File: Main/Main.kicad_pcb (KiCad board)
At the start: 4 copper layers, 76.2 x 64.9 mm, 97 parts, among them J1 USB_B_Micro, J2 XT60, J3 Conn_01x03, J4 Conn_01x03, J5 Conn_01x03, J6 Conn_01x03, J7 MSD-4-A, J9 Conn_01x03, Q2 Si2301CDS, SW1 SW_Push, SW2 SW_Push, U1 RP2350A-QFN60, U10 LM75B, U11 MCS1802GS-50-Z, U12 MCS1802GS-50-Z, U13 MCS1802GS-50-Z, U15 AP62150WU, U2 W25Q128JVS, U3 AMS1117-3.3, U4 MMC5983MA, U5 ICM-42688-P, U6 INA226, U7 KX134-1211, U8 MS5611-01BA, U9 MCS1802GS-50-Z, Y1 ABM8-272-T3

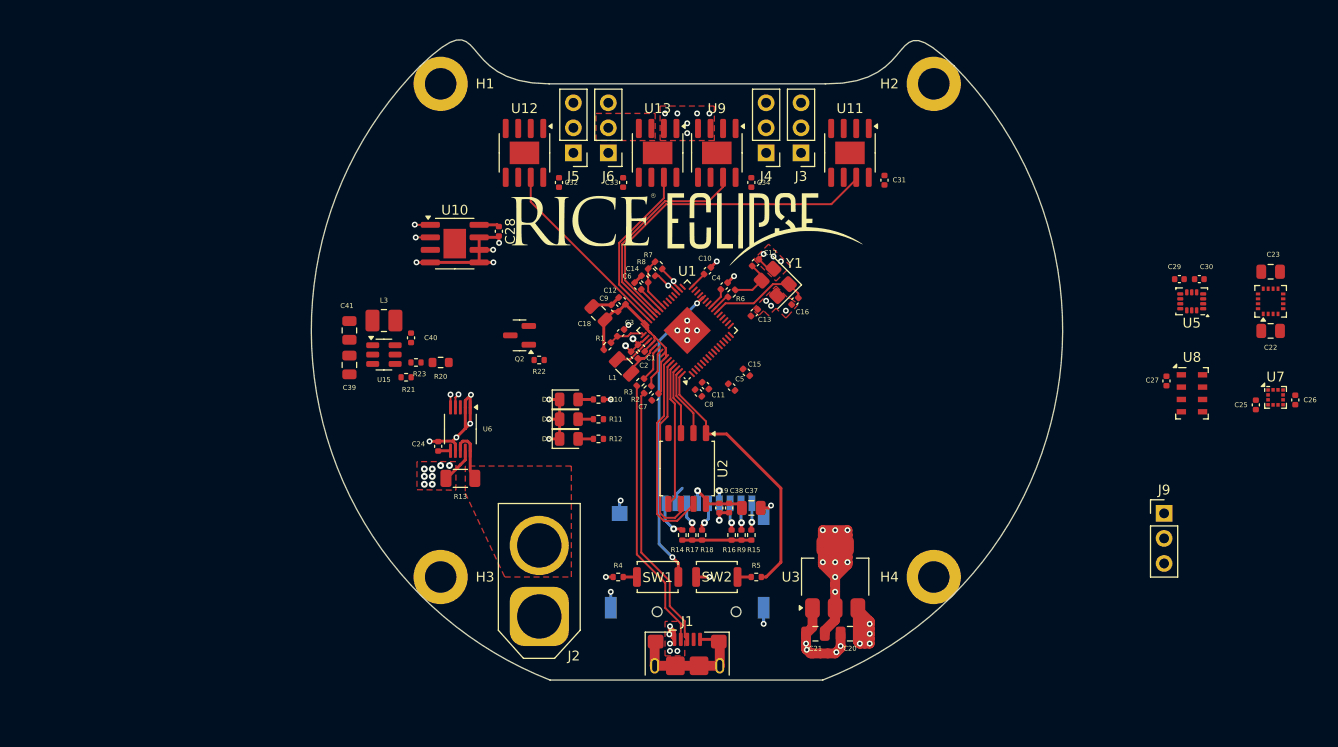
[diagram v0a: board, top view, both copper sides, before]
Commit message: Power Reg Layout Complete
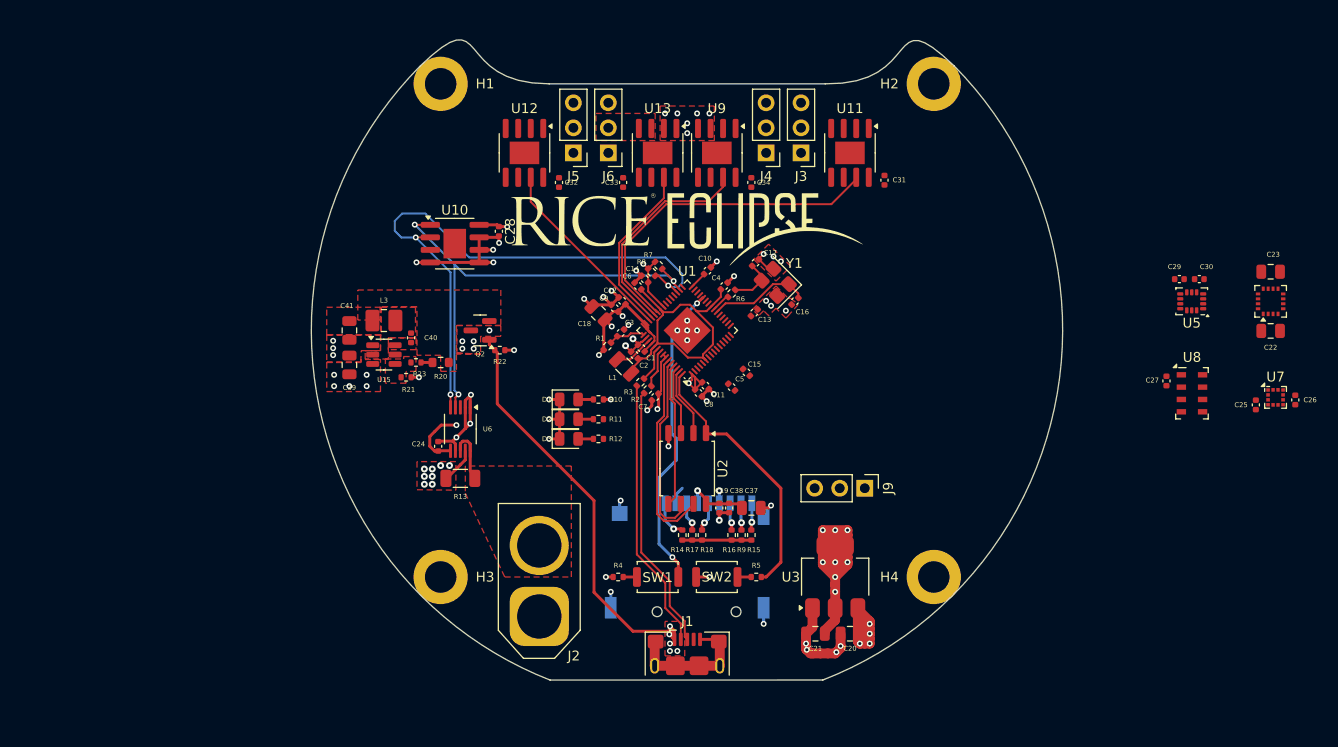
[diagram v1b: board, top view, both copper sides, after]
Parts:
- moved J9 30.5 mm to (118.0, 116.0), turned to -90 degrees
- moved R22 4.11 mm to (81.0, 102.0)
- moved Q2 4.03 mm to (79.0, 100.0)
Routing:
- net SCL: track 5.70 -> 61.0 mm
- net SDA: track 5.92 -> 48.2 mm
- net VBUS: track 16.7 -> 56.0 mm
- net +1V1: track 9.46 -> 32.1 mm
- net +3.3V: track 77.0 -> 90.9 mm, vias 10 -> 23
- net GND: track 82.8 -> 92.8 mm, vias 39 -> 51
- net Net-(R20-Pad2): track 0.00 -> 1.16 mm
- net VIN: vias 14 -> 19
- added copper zone on F.Cu, net +3.3V
- added copper zone on F.Cu, net Net-(Q2-S)
- added copper zone on F.Cu, net Net-(U15-BST)
- added copper zone on F.Cu, net Net-(U15-FB)
- added copper zone on F.Cu, net Net-(U15-SW)

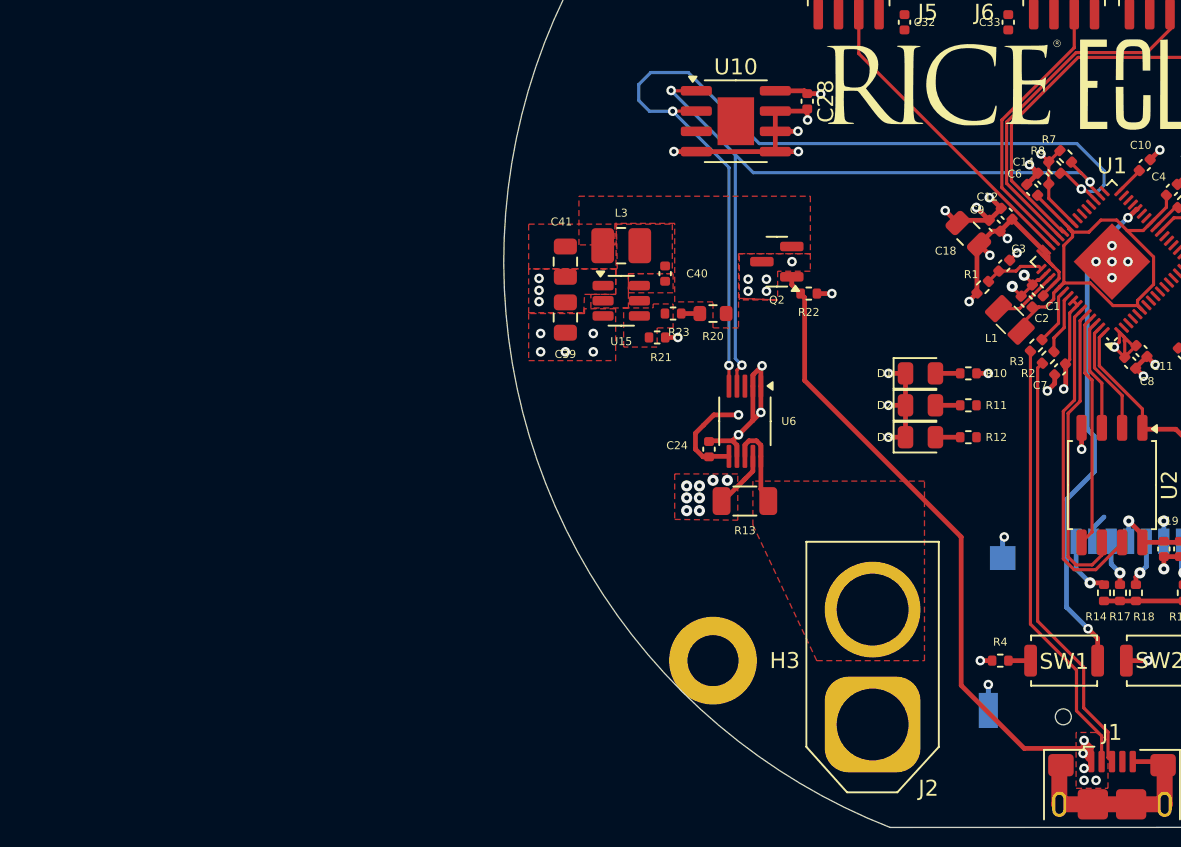
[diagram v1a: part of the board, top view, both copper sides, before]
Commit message: updated power switching schematic
still need to fix footprint tsp
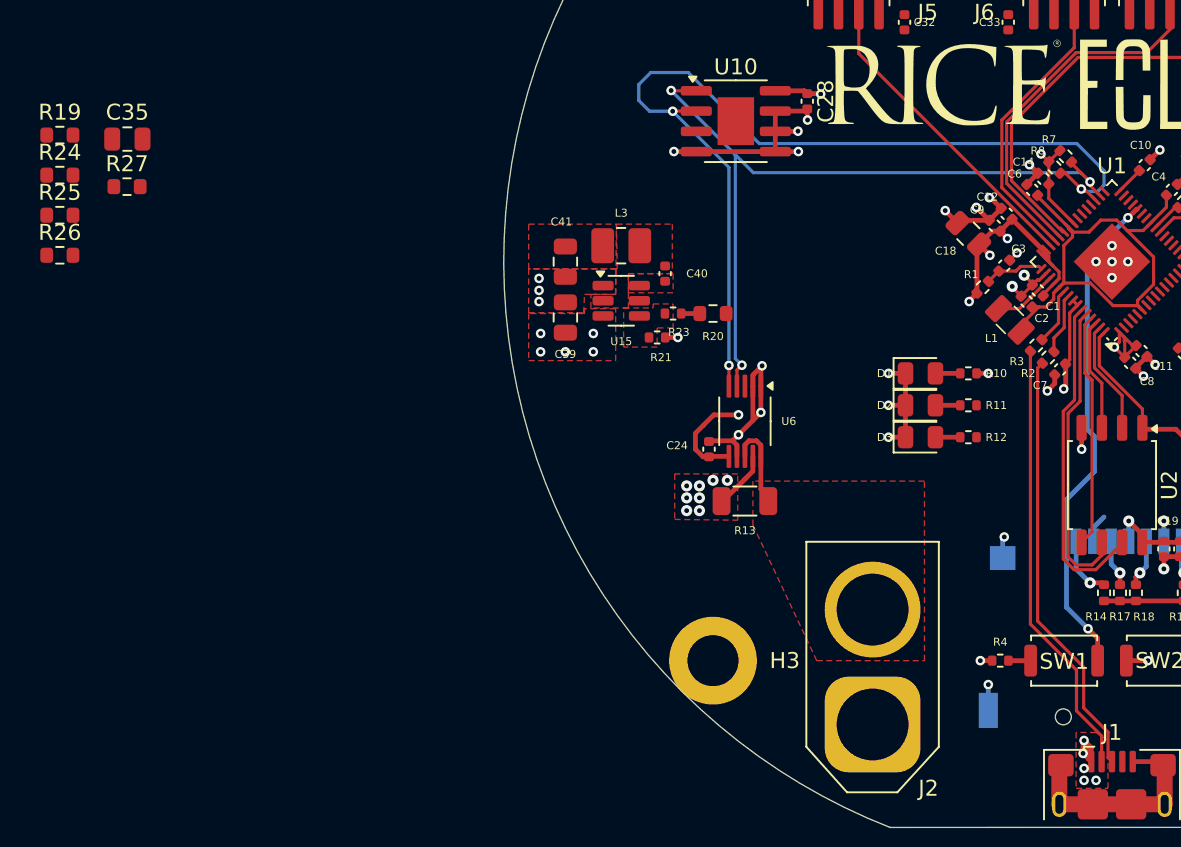
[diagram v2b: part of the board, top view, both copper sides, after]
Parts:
- removed Q2: Si2301CDS, Package_TO_SOT_SMD:SOT-23
- removed R22: 100k, Resistor_SMD:R_0402_1005Metric
- added C35: 1u, Capacitor_SMD:C_0805_2012Metric, F.Cu at (38.3, 92.3)
- added R19: 30k, Resistor_SMD:R_0603_1608Metric, F.Cu at (34.1, 92.1)
- added R24: 100k, Resistor_SMD:R_0603_1608Metric, F.Cu at (34.1, 94.6)
- added R25: 100k, Resistor_SMD:R_0603_1608Metric, F.Cu at (34.1, 97.1)
- added R26: 100k, Resistor_SMD:R_0603_1608Metric, F.Cu at (34.1, 99.6)
- added R27: 30k, Resistor_SMD:R_0603_1608Metric, F.Cu at (38.3, 95.3)
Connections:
- net Net-(Q2-S) renamed 3.3v_Batt
- C21 pad 1: +3.3V -> 3.3v_usb
- U3 pad 2: +3.3V -> 3.3v_usb
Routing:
- net VBUS: track 56.0 -> 16.7 mm
- net +3.3V: track 90.9 -> 61.0 mm, vias 23 -> 15
- net 3.3v_usb: track 0.00 -> 29.9 mm, vias 0 -> 3
- net GND: track 92.8 -> 91.8 mm, vias 51 -> 50
- removed copper zone on F.Cu, net +3.3V

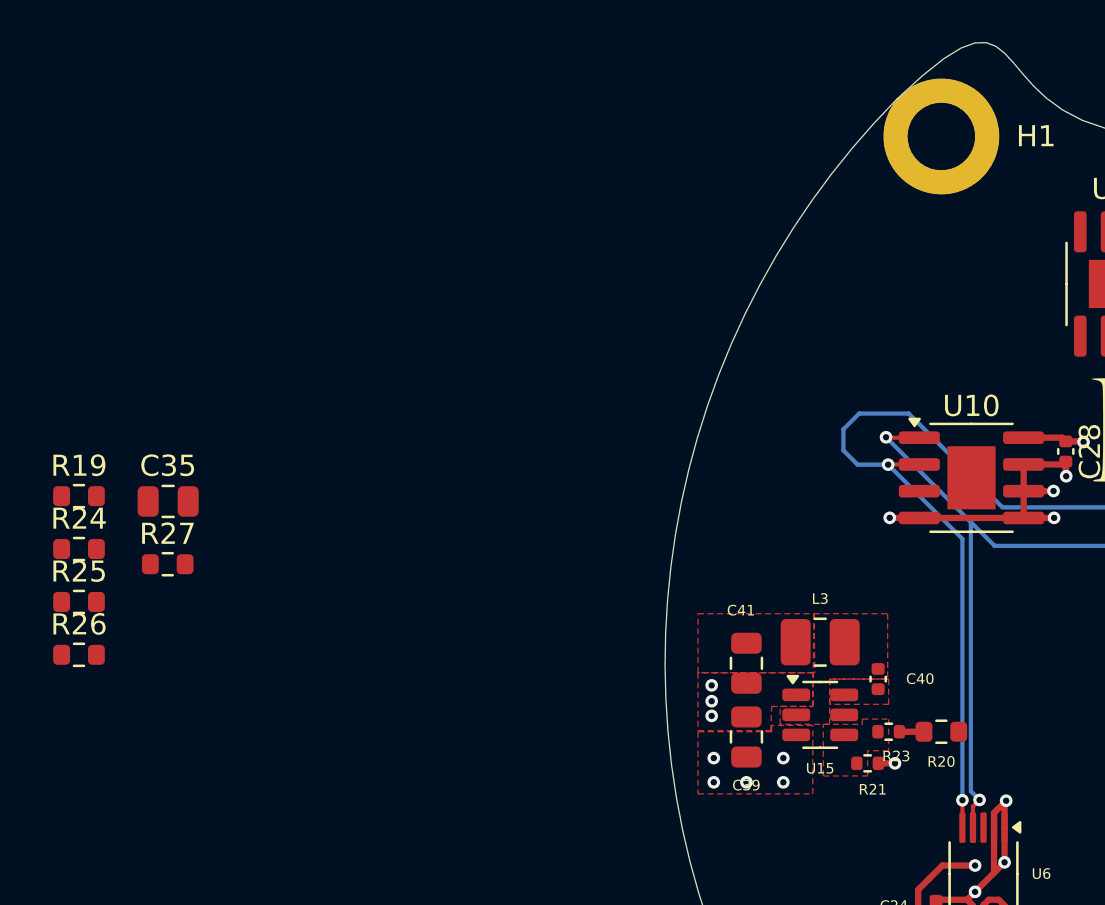
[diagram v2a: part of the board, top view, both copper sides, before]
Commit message: updated power switching circuit
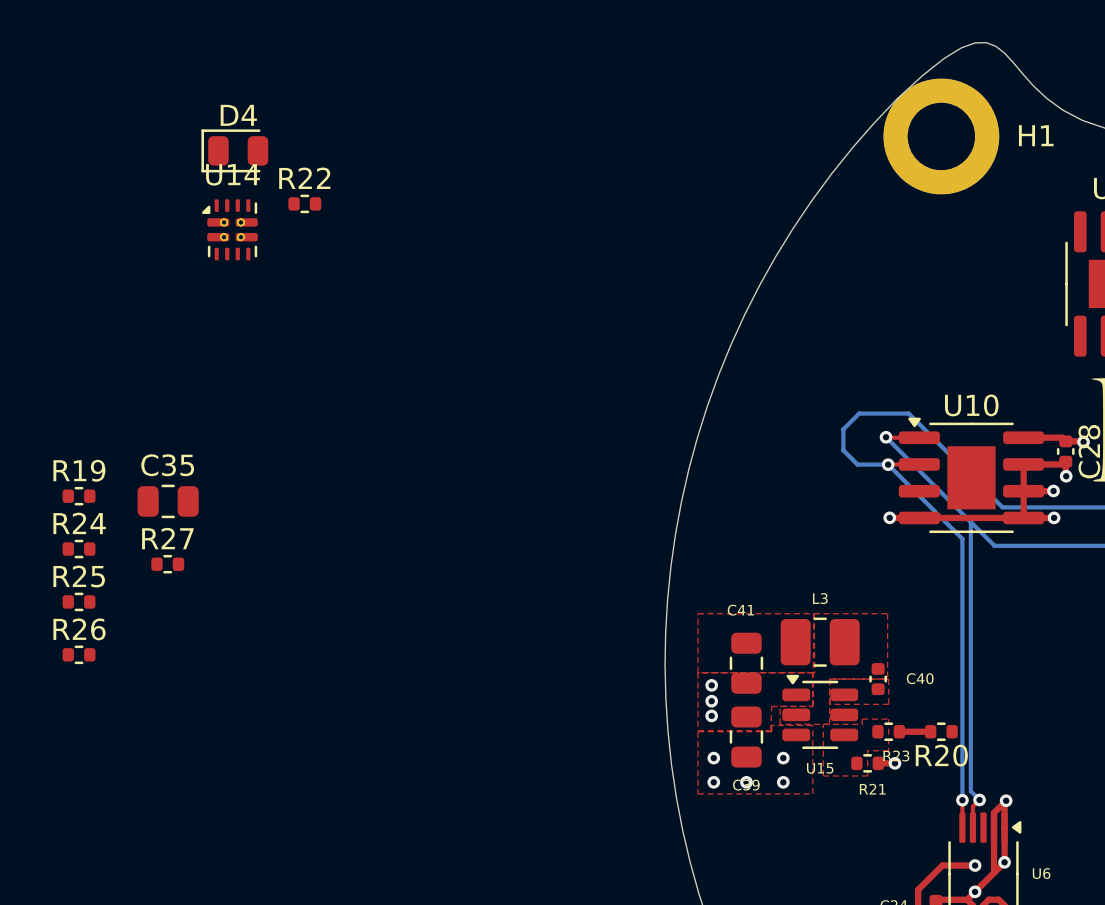
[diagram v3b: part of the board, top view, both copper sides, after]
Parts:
- added D4: RED_LED, LED_SMD:LED_0805_2012Metric, F.Cu at (41.6, 75.7)
- added R22: R, Resistor_SMD:R_0402_1005Metric, F.Cu at (44.8, 78.2)
- added U14: TPS2121RUXR, Package_DFN_QFN:Texas_VQFN-HR-12_2x2.5mm_P0.5mm_ThermalVias, F.Cu at (41.4, 79.4)
- R19, R20, R24, R25, R26: footprint Resistor_SMD:R_0603_1608Metric -> Resistor_SMD:R_0402_1005Metric
- R27: value 30k -> 100k; footprint Resistor_SMD:R_0603_1608Metric -> Resistor_SMD:R_0402_1005Metric

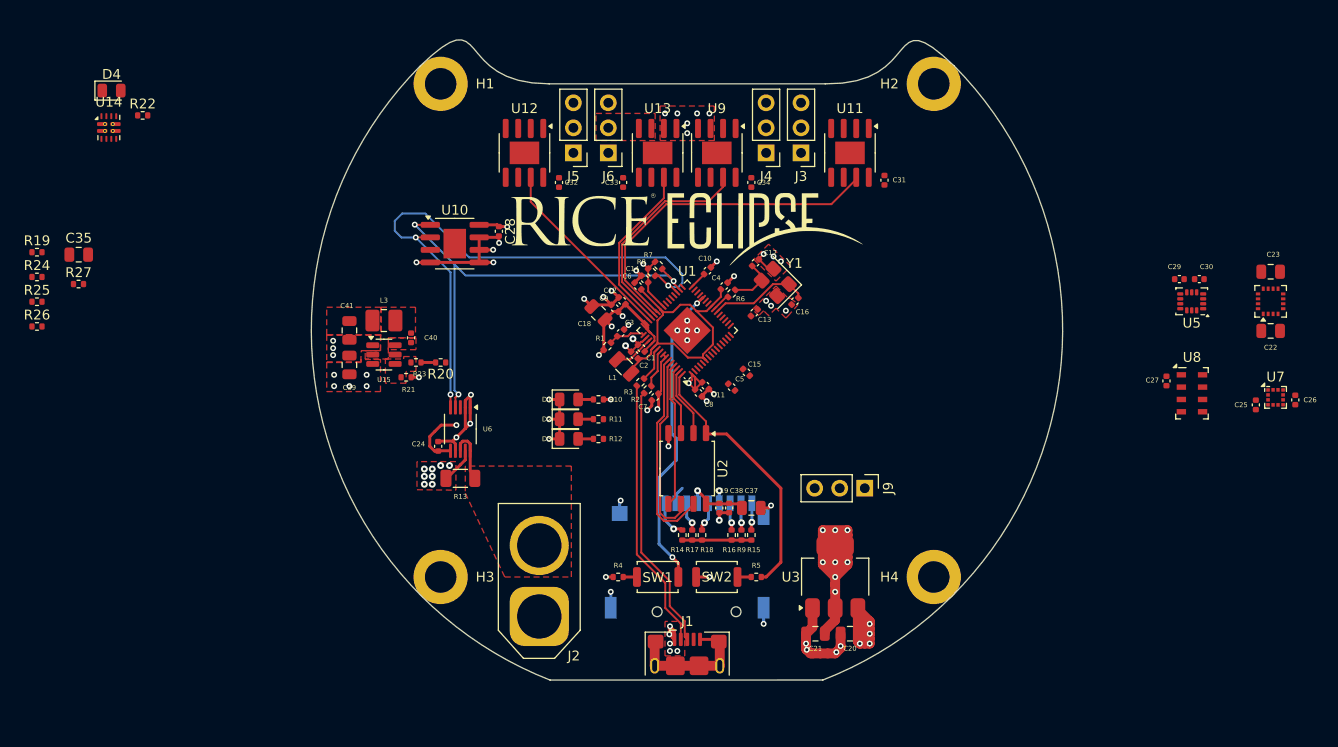
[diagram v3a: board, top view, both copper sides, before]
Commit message: updated power circuit layout
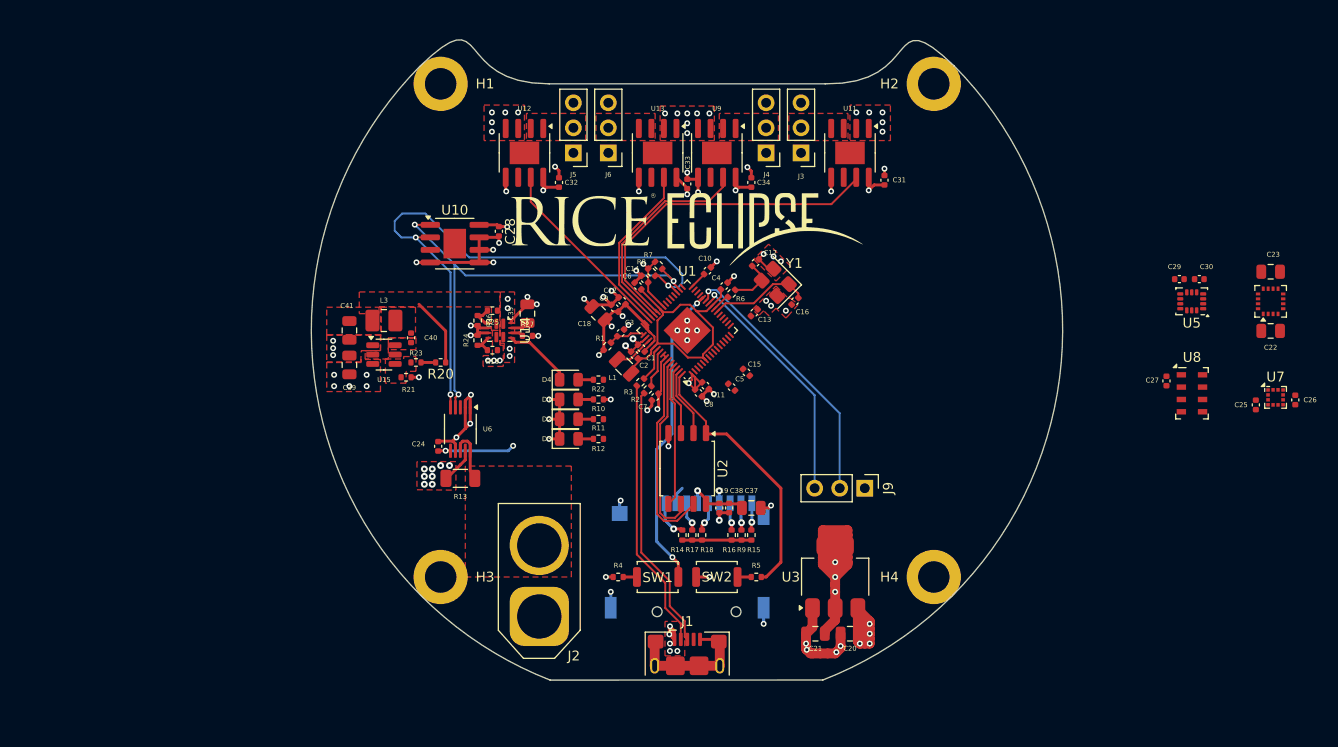
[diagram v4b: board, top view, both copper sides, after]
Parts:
- U14: footprint Package_DFN_QFN:Texas_VQFN-HR-12_2x2.5mm_P0.5mm_ThermalVias -> Package_DFN_QFN:Texas_VQFN-HR-12_2x2.5mm_P0.5mm
- moved D4 54.9 mm to (88.0, 105.0)
- moved R22 53.4 mm to (91.0, 105.0), turned to 180 degrees
- moved R19 47.2 mm to (80.2, 102.0), turned to 180 degrees
- moved R25 46.2 mm to (80.2, 98.0), turned to 180 degrees
- moved C35 45.9 mm to (83.8, 98.3), turned to 90 degrees
- moved R27 45.8 mm to (83.8, 100.5)
- moved R24 45.1 mm to (78.8, 101.0), turned to 90 degrees
- moved R26 44.7 mm to (78.8, 99.0), turned to -90 degrees
- moved U14 44.7 mm to (81.0, 100.0), turned to -90 degrees
- moved C33 6.50 mm to (100.0, 85.2)
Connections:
- D4 pad 2: OUT -> Net-(D4-A)
- R22 pad 1: Net-(D4-K) -> +3.3V
- R22 pad 2: Net-(U14-ST) -> Net-(D4-A)
- U14 pad 1: OUT -> +3.3V
- U14 pad 8: OUT -> +3.3V
- U14 pad 9: Net-(U14-ST) -> Net-(D4-K)
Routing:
- net Net-(J9-Pin_2): track 0.00 -> 27.2 mm, vias 0 -> 1
- net Net-(J9-Pin_3): track 0.00 -> 24.9 mm, vias 0 -> 1
- net GND: track 91.8 -> 112.3 mm, vias 50 -> 63
- net +3.3V: track 61.0 -> 74.3 mm, vias 15 -> 19
- net Net-(D4-K): track 0.00 -> 7.10 mm
- net 3.3v_Batt: track 0.00 -> 7.02 mm
- net Net-(U14-PR1): track 0.00 -> 2.61 mm
- net Net-(U14-CP2): track 0.00 -> 2.61 mm
- net Net-(U14-SS): track 0.00 -> 1.86 mm
- net Net-(D4-A): track 0.00 -> 1.55 mm
- net Net-(U14-ILIM): track 0.00 -> 1.26 mm
- net VIN: vias 19 -> 30
- net 3.3v_usb: vias 3 -> 6
- added copper zone on F.Cu, net +3.3V
- added copper zone on F.Cu, net 3.3v_usb
- added copper zone on In2.Cu, net 3.3v_usb
- added copper zone on F.Cu, net current -1
- added copper zone on F.Cu, net current -2
- added copper zone on F.Cu, net current -3
